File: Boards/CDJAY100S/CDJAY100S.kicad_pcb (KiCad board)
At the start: 2 copper layers, 150 x 185 mm, 74 parts, among them CN701 52492-3620, CN705 52151-1410, J1 Rotary Encoder, U1 PT6324Q, U2 TXS0108EPW, U3 CH334R, X1 12MHz

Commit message: Updated the board to have an own power supply for the DAC, and an own ADC for the Pitch fader
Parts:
- removed C1, C4: 100 n, Capacitor_SMD:C_1206_3216Metric_Pad1.33x1.80mm_HandSolder
- removed C2, C3: 10 u, Capacitor_SMD:C_1206_3216Metric_Pad1.33x1.80mm_HandSolder
- removed CR2: MBR120VLSFT1G, Diode_SMD:Nexperia_CFP3_SOD-123W
- removed R1, R5: 10 k, Resistor_SMD:R_1206_3216Metric_Pad1.30x1.75mm_HandSolder
- removed R14, R32, R33, R34: 10k, Resistor_SMD:R_1206_3216Metric_Pad1.30x1.75mm_HandSolder
- removed R2, R6: 20 k, Resistor_SMD:R_1206_3216Metric_Pad1.30x1.75mm_HandSolder
- removed R3, R4: 5.1 k, Resistor_SMD:R_1206_3216Metric_Pad1.30x1.75mm_HandSolder
- added C18: 1200 p, Capacitor_SMD:C_1206_3216Metric_Pad1.33x1.80mm_HandSolder, F.Cu at (189.2, 72.7)
- added C20: 100 n, Capacitor_SMD:C_1206_3216Metric_Pad1.33x1.80mm_HandSolder, F.Cu at (186.5, 143.6)
- added C25: 100 n, Capacitor_SMD:C_1206_3216Metric_Pad1.33x1.80mm_HandSolder, F.Cu at (198.5, 40.2)
- added C26: 10 u, Capacitor_SMD:C_1206_3216Metric_Pad1.33x1.80mm_HandSolder, F.Cu at (193.8, 35.2)
- added C27: 100 n, Capacitor_SMD:C_1206_3216Metric_Pad1.33x1.80mm_HandSolder, F.Cu at (177.2, 105.2)
- added C28: 100 n, Capacitor_SMD:C_1206_3216Metric_Pad1.33x1.80mm_HandSolder, F.Cu at (177.2, 99.0)
- added C29: 10 u, Capacitor_SMD:C_1206_3216Metric_Pad1.33x1.80mm_HandSolder, F.Cu at (188.5, 35.2)
- added C30: 10 u, Capacitor_SMD:C_1206_3216Metric_Pad1.33x1.80mm_HandSolder, F.Cu at (188.5, 37.8)
- added C31: 10 u, Capacitor_SMD:C_1206_3216Metric_Pad1.33x1.80mm_HandSolder, F.Cu at (198.5, 45.5)
- added C32: 10 u, Capacitor_SMD:C_1206_3216Metric_Pad1.33x1.80mm_HandSolder, F.Cu at (196.0, 24.8)
- added C33: 10 u, Capacitor_SMD:C_1206_3216Metric_Pad1.33x1.80mm_HandSolder, F.Cu at (192.8, 24.7)
- added C34: 100 n, Capacitor_SMD:C_1206_3216Metric_Pad1.33x1.80mm_HandSolder, F.Cu at (181.2, 106.8)
- added CNT2: MBR120VLSFT1G, Diode_SMD:Nexperia_CFP3_SOD-123W, F.Cu at (183.4, 33.2)
- added U4: AP2127K-3.3, Package_TO_SOT_SMD:SOT-23-5, F.Cu at (193.8, 29.8)
- added U5: TXS0108EPW, Package_SO:TSSOP-20_4.4x6.5mm_P0.65mm, F.Cu at (170.6, 101.4)
- added U6: ADS1115IDGS, Package_SO:TSSOP-10_3x3mm_P0.5mm, F.Cu at (183.6, 102.2)
- C16: value 1 u -> 110 n
- JP1: value (none) -> SolderJumper_2_Open
- R10, R11, R9: value 10 k -> 10k
- U2: value TXS0108EPW -> TXB0108PW
- moved R13 28.8 mm to (183.8, 91.2), turned to 90 degrees
- moved R12 28.0 mm to (180.0, 91.0), turned to 90 degrees
- moved D14 19.3 mm to (183.2, 79.5), turned to -90 degrees
- moved D16 15.5 mm to (180.0, 79.5), turned to -90 degrees
- moved D15 13.8 mm to (183.2, 85.2), turned to -90 degrees
- moved D13 11.7 mm to (180.0, 85.2), turned to -90 degrees
- moved C14 5.62 mm to (186.5, 41.8), turned to -90 degrees
- moved C13 4.76 mm to (181.8, 41.2)
- moved C11 4.51 mm to (181.8, 38.5)
- moved C15 4.09 mm to (185.5, 47.5), turned to -90 degrees
- moved C16 2.85 mm to (193.8, 37.8), turned to 180 degrees
- moved C5 2.35 mm to (189.5, 84.2)
- moved C6 1.58 mm to (189.5, 90.0)
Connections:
- C11 pad 1: +3V3 -> +3V3A
- C11 pad 2: Net-(i2S_Audio1-CPVDD) -> GNDA
- C13 pad 1: +3V3 -> +3V3A
- C13 pad 2: Net-(i2S_Audio1-AVDD) -> GNDA
- C16 pad 2: GND -> GNDA
- CN701 pad 2: Net-(CN701-ADIN) -> /ADIN
- R12 pad 1: Net-(rPi1-GPIO15) -> /CNT2
- R13 pad 1: Net-(rPi1-GPIO22) -> /CNT1
- i2S_Audio1 pad 1: Net-(i2S_Audio1-CPVDD) -> +3V3A
- i2S_Audio1 pad 11: +3V3 -> +3V3A
- i2S_Audio1 pad 20: Net-(i2S_Audio1-CPVDD) -> +3V3
- i2S_Audio1 pad 3: GND -> GNDA
- i2S_Audio1 pad 8: Net-(i2S_Audio1-AVDD) -> +3V3A
- rPi1 pad 20: Net-(rPi1-GPIO15) -> Net-(U5-A3)
- rPi1 pad 29: Net-(rPi1-GPIO22) -> Net-(U5-A2)
- rPi1 pad 31: /ADIN -> Net-(U5-A7)
- rPi1 pad 32: /CT -> Net-(U5-A8)
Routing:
- net Net-(CN701-ADIN): track 80.9 -> 0.00 mm
- net +3V3: track 220.6 -> 291.1 mm, vias 2 -> 6
- net Net-(U5-A8): track 0.00 -> 64.3 mm, vias 0 -> 3
- net Net-(U5-A7): track 0.00 -> 59.8 mm, vias 0 -> 3
- net Net-(U5-A2): track 0.00 -> 58.8 mm, vias 0 -> 1
- net /CT: track 57.2 -> 0.00 mm, vias 1 -> 0
- net GNDA: track 44.2 -> 96.0 mm, vias 2 -> 1
- net +3V3A: track 0.00 -> 44.4 mm, vias 0 -> 4
- net Net-(U5-A3): track 0.00 -> 42.4 mm, vias 0 -> 1
- net +5V: track 352.6 -> 392.6 mm, vias 5 -> 8
- net Net-(rPi1-GPIO22): track 38.1 -> 0.00 mm, vias 1 -> 0
- net /CNT1: track 0.00 -> 33.6 mm
- net /CNT2: track 0.00 -> 32.2 mm
- net Net-(U5-B7): track 0.00 -> 26.1 mm
- net Net-(CN705-CONT2): track 46.7 -> 21.3 mm, vias 2 -> 0
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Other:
- board text added: "CDJay 100 USB Mainboard V1.6 applab.fh-aachen.de Write it, load it, run it, save it Check it, change it, quick - reuse it"
- board text removed: "CDJay 100 USB Mainboard V1.5 applab.fh-aachen.de Write it, load it, run it, save it Check it, change it, quick - reuse it"

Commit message: Reorganize some traces
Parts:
- moved C7 5.95 mm to (107.8, 42.8)
- moved C9 5.59 mm to (107.8, 40.2)
- moved C8 5.57 mm to (107.8, 37.8)
- moved X1 5.38 mm to (101.7, 32.4), turned to 180 degrees
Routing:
- net GND: track 597.6 -> 619.8 mm
- net +3V3: track 291.1 -> 277.8 mm
- net Net-(U2-A1): track 52.3 -> 46.3 mm
- net Net-(D10-K): track 69.4 -> 75.5 mm
- net Net-(D12-K): track 73.3 -> 78.4 mm
- net Net-(D11-K): track 73.2 -> 77.7 mm
- net Net-(D9-K): track 67.6 -> 71.5 mm
- net +5V: track 392.6 -> 389.0 mm
- net Net-(D8-K): track 63.6 -> 66.3 mm
- net Net-(J1-SW): track 87.2 -> 89.9 mm
- net Net-(U3-XO): track 6.58 -> 8.67 mm
- net /SPI0 TX: track 60.9 -> 62.9 mm
- net Net-(J1-CLK): track 79.0 -> 80.8 mm
- net /SPI0 SCK: track 64.5 -> 66.1 mm
- net /SPI0 CS: track 72.1 -> 73.3 mm
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
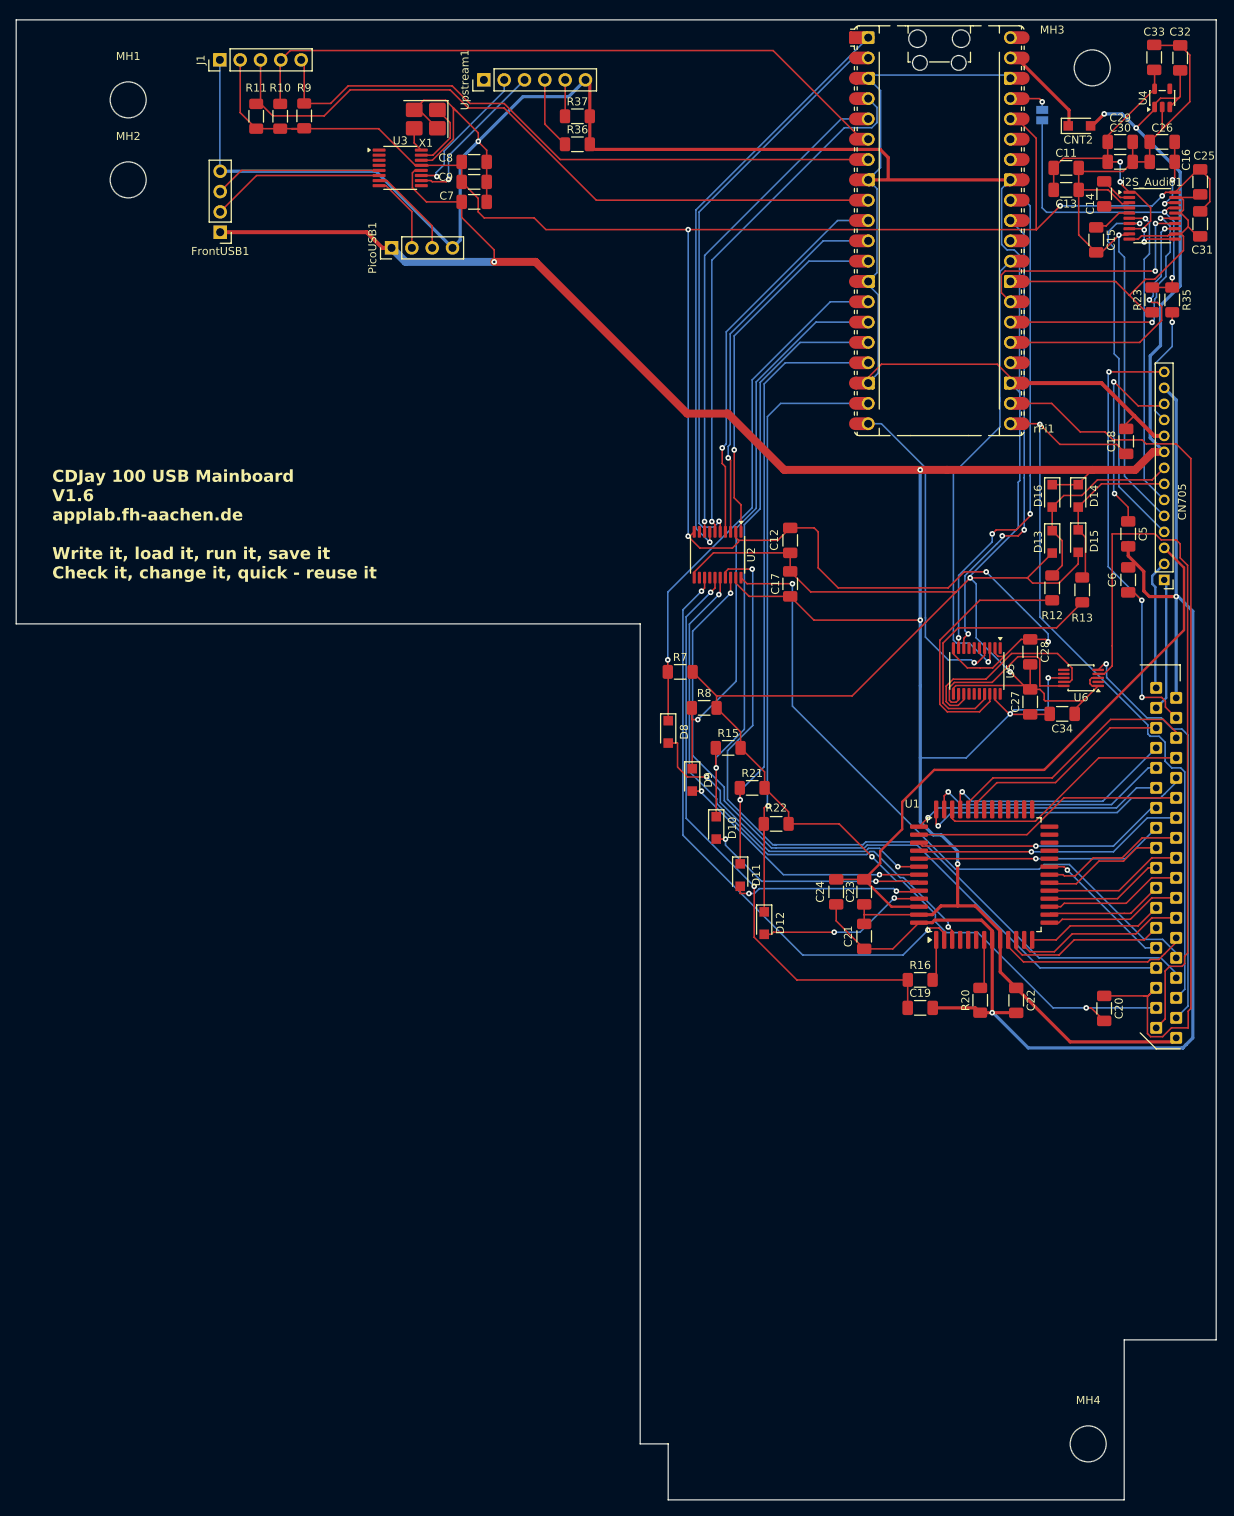
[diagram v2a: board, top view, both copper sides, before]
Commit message: Renamed the components to consistent placement
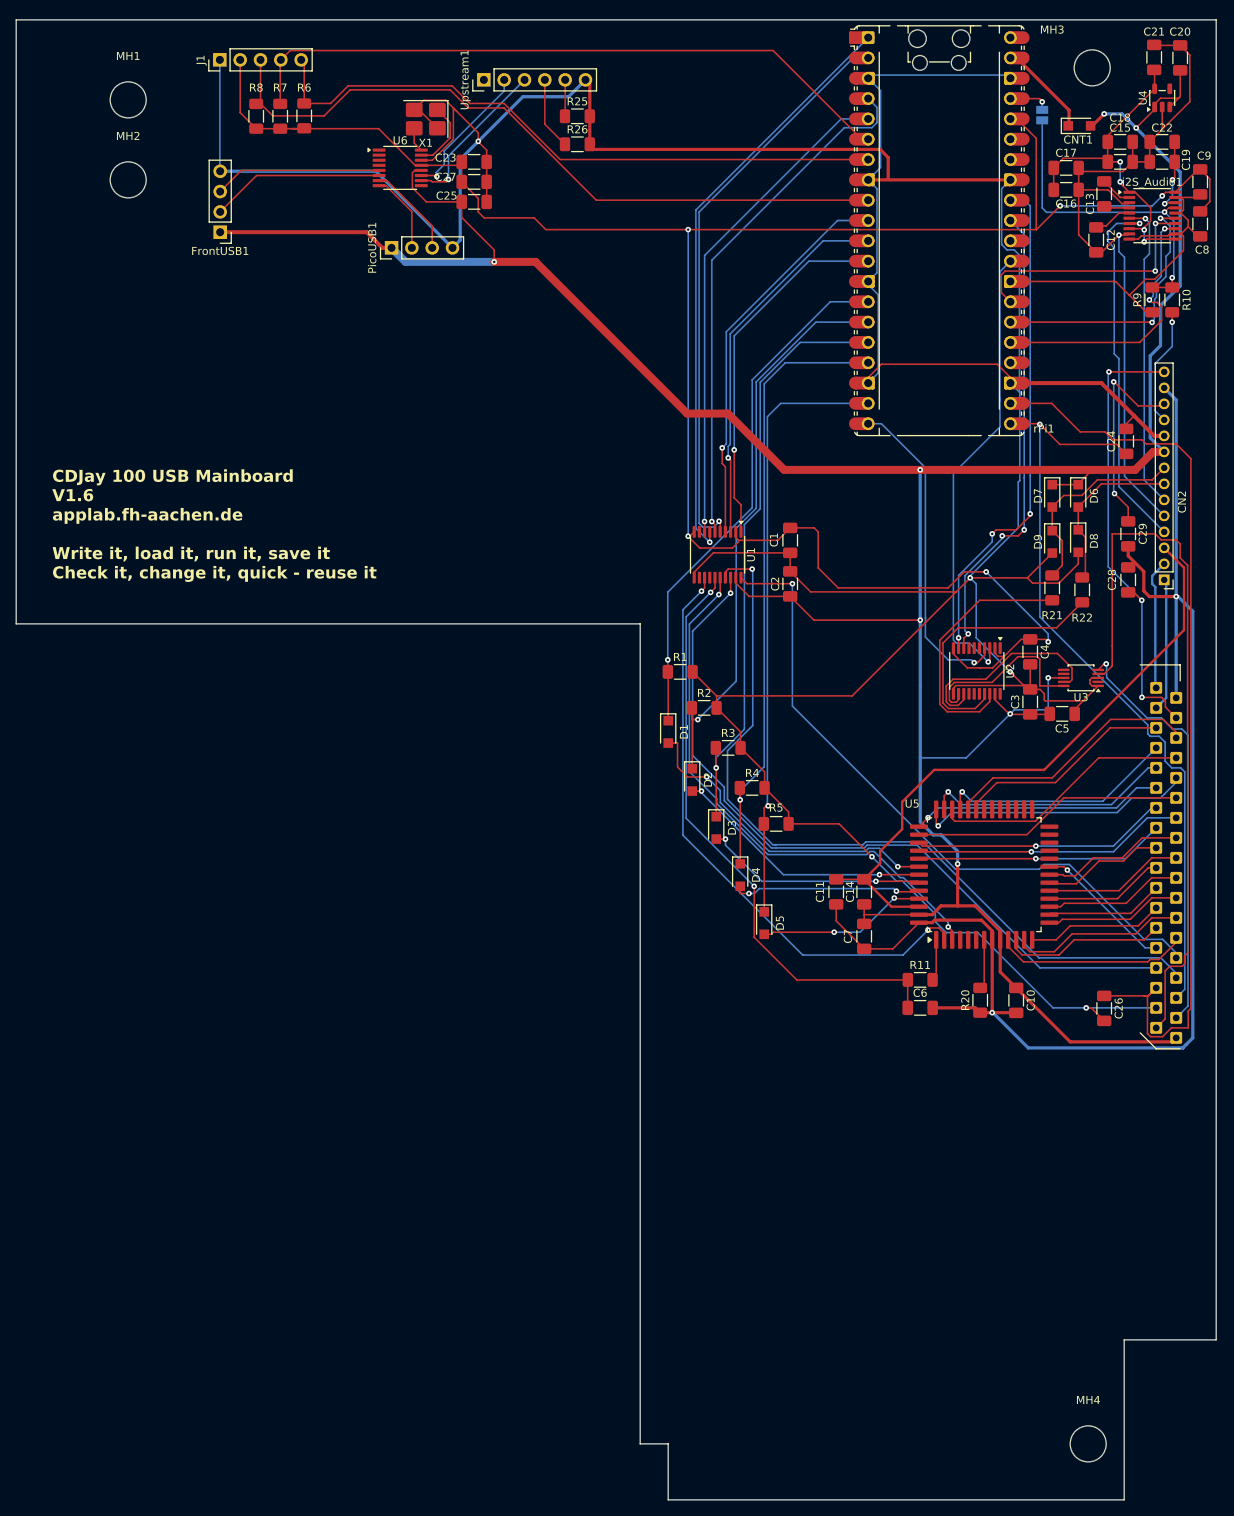
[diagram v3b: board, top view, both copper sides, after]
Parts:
- renumbered C12 to C1, C22 to C10, C24 to C11, C15 to C12, C14 to C13, C23 to C14, C30 to C15, C13 to C16, C11 to C17, C29 to C18, C16 to C19, C17 to C2, C32 to C20, C33 to C21, C26 to C22, C8 to C23, C18 to C24, C7 to C25, C20 to C26, C9 to C27, C6 to C28, C5 to C29, C27 to C3, C28 to C4, C34 to C5, C19 to C6, C21 to C7, C31 to C8, C25 to C9, CN701 to CN1, CN705 to CN2, CNT2 to CNT1, D8 to D1, D9 to D2, D10 to D3, D11 to D4, D12 to D5, D14 to D6, D16 to D7, D15 to D8, D13 to D9, R7 to R1, R35 to R10, R16 to R11, R8 to R2, R12 to R21, R13 to R22, R37 to R25, R36 to R26, R15 to R3, R21 to R4, R22 to R5, R9 to R6, R10 to R7, R11 to R8, R23 to R9, U2 to U1, U5 to U2, U6 to U3, U1 to U5, U3 to U6
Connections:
- rPi1 pad 13: GND -> Net-(rPi1-GND-Pad13)
- rPi1 pad 18: GND -> Net-(rPi1-GND-Pad13)
- rPi1 pad 23: GND -> Net-(rPi1-GND-Pad13)
- rPi1 pad 28: GND -> Net-(rPi1-GND-Pad13)
- rPi1 pad 3: GND -> Net-(rPi1-GND-Pad13)
- rPi1 pad 38: GND -> Net-(rPi1-GND-Pad13)
- rPi1 pad 8: GND -> Net-(rPi1-GND-Pad13)

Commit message: Version 1.6
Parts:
- removed C3, C4: 100 n, Capacitor_SMD:C_1206_3216Metric_Pad1.33x1.80mm_HandSolder
- removed U2: TXS0108EPW, Package_SO:TSSOP-20_4.4x6.5mm_P0.65mm
- C26: value 100 n -> 1200 p
- C27: value 1uf -> 1u
- U1: value TXB0108PW -> TXS0108
- moved C26 75.1 mm to (185.2, 68.5)
- moved U3 42.6 mm to (141.5, 96.0), turned to 90 degrees
- moved C5 40.2 mm to (144.5, 90.5), turned to -90 degrees
- moved R21 9.62 mm to (176.0, 82.2), turned to 0 degrees
- moved R22 7.38 mm to (180.2, 84.8), turned to 0 degrees
- moved D8 3.35 mm to (183.2, 88.5)
- moved D9 3.25 mm to (180.0, 88.5)
- turned C2 to -90 degrees
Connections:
- C2 pad 1: +5V -> GND
- C2 pad 2: GND -> +5V
- C26 pad 1: /JOG2 -> GND
- C26 pad 2: GND -> /JOG2
- U1 pad 12: unconnected-(U1-B8-Pad12) -> /STB
- U1 pad 16: /STB -> /CNT1
- U1 pad 17: Net-(CN1-KD2) -> /CNT2
- U1 pad 18: Net-(CN1-KD1) -> Net-(U1-B2)
- U1 pad 20: /KD0 -> Net-(U1-B1)
- U1 pad 5: /SPI0 CS -> Net-(U1-A4)
- U1 pad 9: unconnected-(U1-A8-Pad9) -> /SPI0 CS
- U3 pad 10: Net-(U2-B8) -> Net-(U1-B2)
- U3 pad 9: Net-(U2-B7) -> Net-(U1-B1)
- rPi1 pad 10: Net-(U1-A3) -> Net-(CN1-KD2)
- rPi1 pad 11: Net-(U1-A2) -> Net-(CN1-KD1)
- rPi1 pad 12: Net-(U1-A1) -> /KD0
- rPi1 pad 13: Net-(rPi1-GND-Pad13) -> GND
- rPi1 pad 18: Net-(rPi1-GND-Pad13) -> GND
- rPi1 pad 20: Net-(U2-A3) -> Net-(U1-A4)
- rPi1 pad 23: Net-(rPi1-GND-Pad13) -> GND
- rPi1 pad 28: Net-(rPi1-GND-Pad13) -> GND
- rPi1 pad 29: Net-(U2-A2) -> Net-(U1-A3)
- rPi1 pad 3: Net-(rPi1-GND-Pad13) -> GND
- rPi1 pad 31: Net-(U2-A7) -> Net-(U1-A1)
- rPi1 pad 32: Net-(U2-A8) -> Net-(U1-A2)
- rPi1 pad 38: Net-(rPi1-GND-Pad13) -> GND
- rPi1 pad 8: Net-(rPi1-GND-Pad13) -> GND
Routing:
- net Net-(U2-A8): track 64.3 -> 0.00 mm, vias 3 -> 0
- net Net-(U2-A7): track 59.8 -> 0.00 mm, vias 3 -> 0
- net Net-(U2-A2): track 58.8 -> 0.00 mm, vias 1 -> 0
- net +3V3: track 277.8 -> 220.1 mm, vias 6 -> 4
- net Net-(U2-A3): track 42.4 -> 0.00 mm, vias 1 -> 0
- net Net-(CN1-CT): track 52.1 -> 89.8 mm, vias 1 -> 2
- net /KD0: track 83.9 -> 119.9 mm
- net GND: track 619.8 -> 585.7 mm, vias 5 -> 6
- net Net-(U1-A2): track 47.8 -> 79.4 mm
- net Net-(CN1-KD2): track 100.6 -> 128.5 mm
- net Net-(U1-A1): track 46.3 -> 73.2 mm
- net Net-(CN1-KD1): track 94.4 -> 121.1 mm
- net Net-(U2-B7): track 26.1 -> 0.00 mm
- net Net-(U1-A4): track 0.00 -> 25.3 mm, vias 0 -> 2
- net +5V: track 389.0 -> 364.3 mm, vias 8 -> 6
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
